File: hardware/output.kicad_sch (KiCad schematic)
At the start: 27 parts, among them J6 Conn_Coaxial, U19 ADL5611, U20 HMC624A, U21 ADL5611

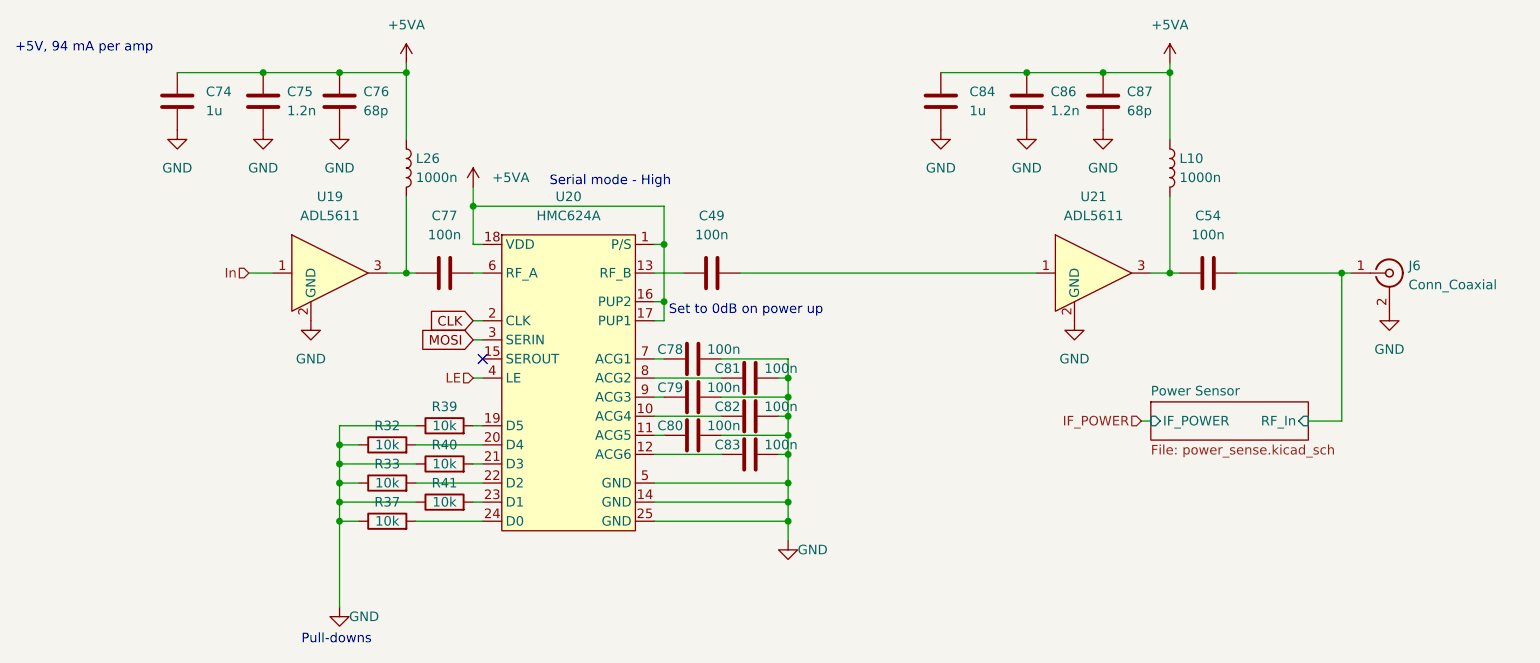
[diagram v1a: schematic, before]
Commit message: Remove cal circuit, swap attens, swap norflash
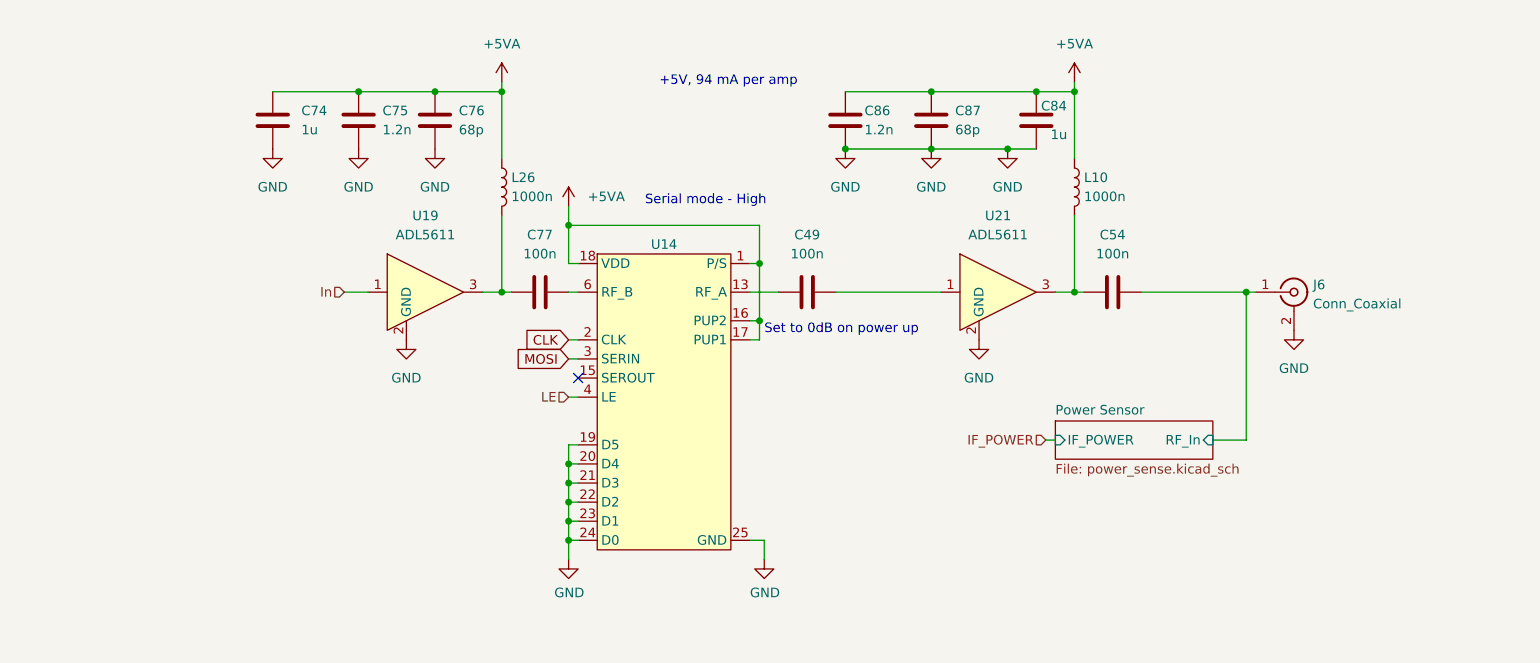
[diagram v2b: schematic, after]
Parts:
- removed C78, C79, C80, C81, C82, C83: 100n, Capacitor_SMD:C_0402_1005Metric, symbol Device:C
- removed R32, R33, R37, R39, R40, R41: 10k, Resistor_SMD:R_0402_1005Metric, symbol Device:R
- removed U20: HMC624A, Package_CSP:LFCSP-24-1EP_4x4mm_P0.5mm_EP2.5x2.5mm, symbol Project Library:HMC624A
- added U14: HMC1122, Package_CSP:LFCSP-24-1EP_4x4mm_P0.5mm_EP2.5x2.5mm, symbol DSA2K:HMC1122
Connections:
- net +5VA: now also U14.1 (P/S), U14.16 (PUP2), U14.17 (PUP1), U14.18 (VDD)
- net CLK: now also U14.2 (CLK)
- net GND: now also U14.10 (GND), U14.11 (GND), U14.12 (GND), U14.14 (GND), U14.19 (D5), U14.20 (D4), U14.21 (D3), U14.22 (D2), U14.23 (D1), U14.24 (D0), U14.25 (GND), U14.5 (GND), U14.7 (GND), U14.8 (GND), U14.9 (GND)
- net LE: now also U14.4 (LE)
- net MOSI: now also U14.3 (SERIN)
- net at C77.2: now also U14.6 (RF_B)
- net at C49.1: now also U14.13 (RF_A)
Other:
- note removed: "Pull-downs"
- moved on the sheet: C49, C54, C74, C75, C76, C77, C84, C86, C87, J6, L10, L26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

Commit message: Update FEM hardware design for production version
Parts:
- renumbered C74 to C54, C75 to C55, C76 to C56, C77 to C57, C49 to C58, C86 to C59, C87 to C60, C84 to C61, C54 to C62, J6 to J7, L26 to L24, L10 to L25, U14 to U12, U19 to U14, U21 to U16
